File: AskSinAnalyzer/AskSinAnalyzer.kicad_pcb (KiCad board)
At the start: 2 copper layers, 87.6 x 57.8 mm, 14 parts, among them J1 Supply, SW1 SW_DIP_x04, SW2 SW_Push, U1 ESP-WROOM-32_DEVKIT_V4, U2 Arduino_Pro_Mini, U3 CC1101, U4 TJCTM24028-SPI

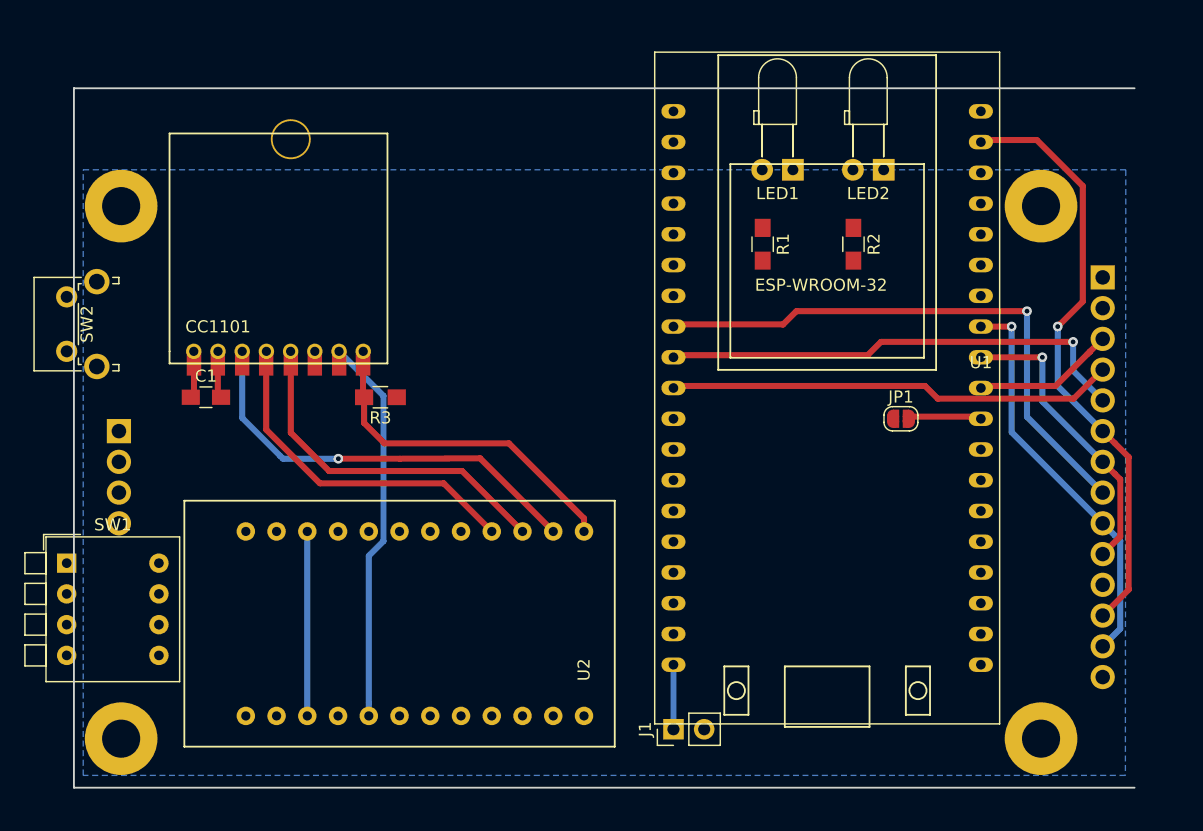
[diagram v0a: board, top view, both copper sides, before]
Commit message: AskSinAnalyzer PCB
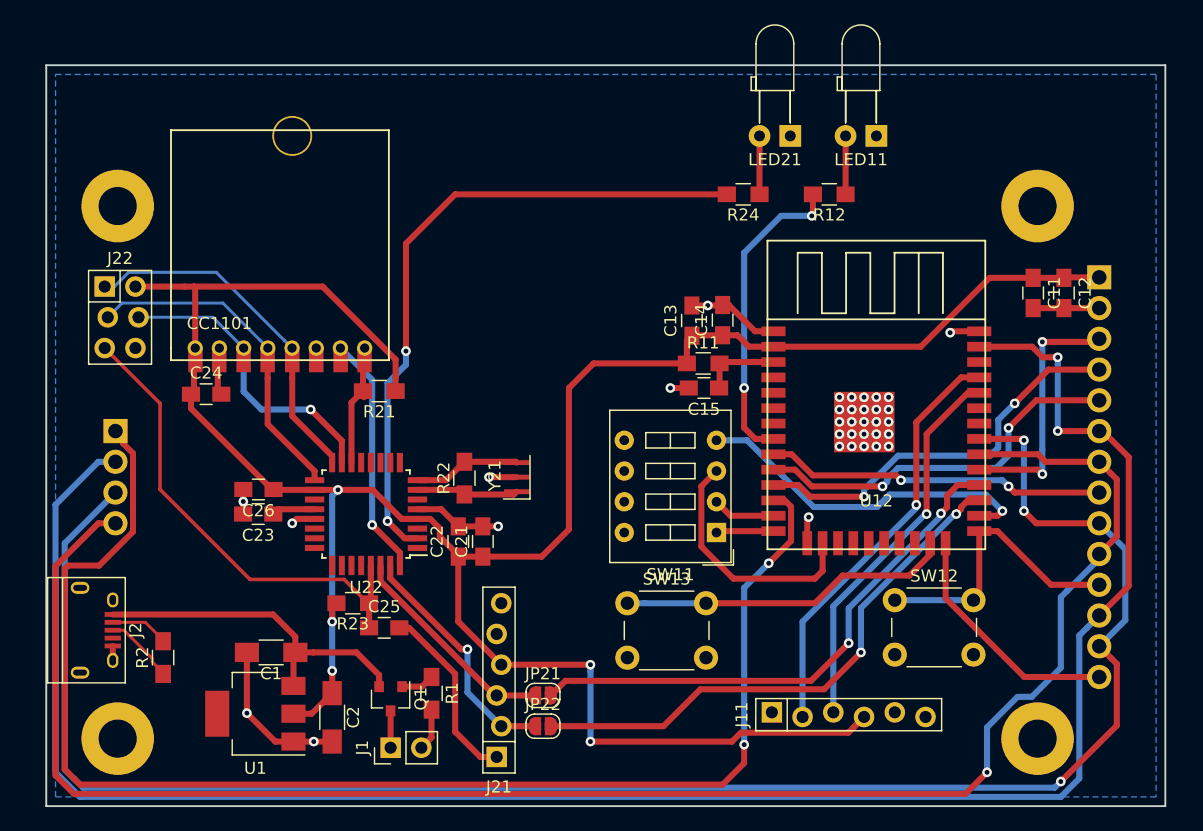
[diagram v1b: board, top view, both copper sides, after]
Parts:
- removed JP1: ~, Jumper:SolderJumper-2_P1.3mm_Open_RoundedPad1.0x1.5mm
- removed LED1: GREEN, LEDs:LED_D3.0mm_Horizontal_O3.81mm_Z6.0mm
- removed LED2: YELLOW, LEDs:LED_D3.0mm_Horizontal_O3.81mm_Z6.0mm
- removed R3: 10k, Resistors_SMD:R_0805_HandSoldering
- removed SW1: SW_DIP_x04, Buttons_Switches_THT:SW_DIP_x4_W7.62mm_Piano
- removed SW2: SW_Push, Buttons_Switches_THT:SW_Tactile_SPST_Angled_PTS645Vx83-2LFS
- removed U2: Arduino_Pro_Mini, myArduinoModules:Arduino_Pro_Mini_wo_Ax
- removed U3: CC1101, CC1101_Module:CC1101_Module
- removed U4: TJCTM24028-SPI, myDisplays:TJCTM24028-SPI
- added C11: 10u, Capacitors_SMD:C_0805_HandSoldering, F.Cu at (117.3, 105.2)
- added C12: 100n, Capacitors_SMD:C_0805_HandSoldering, F.Cu at (119.9, 105.2)
- added C13: 10u, Capacitors_SMD:C_0805_HandSoldering, F.Cu at (89.2, 107.5)
- added C14: 100n, Capacitors_SMD:C_0805_HandSoldering, F.Cu at (91.7, 107.4)
- added C15: 100n, Capacitors_SMD:C_0805_HandSoldering, F.Cu at (90.2, 113.0)
- added C2: 22u, Capacitors_SMD:C_1206_HandSoldering, F.Cu at (59.4, 140.2)
- added C21: 10u, Capacitors_SMD:C_0805_HandSoldering, F.Cu at (71.9, 125.7)
- added C22: 100n, Capacitors_SMD:C_0805_HandSoldering, F.Cu at (69.8, 125.7)
- added C23: 100n, Capacitors_SMD:C_0805_HandSoldering, F.Cu at (53.3, 123.4)
- added C24: 1u, Capacitors_SMD:C_0805_HandSoldering, F.Cu at (49.0, 113.5)
- added C25: 100n, Capacitors_SMD:C_0805_HandSoldering, F.Cu at (63.7, 132.8)
- added C26: 100n, Capacitors_SMD:C_0805_HandSoldering, F.Cu at (53.3, 121.4)
- added J11: FTDI_ESP, myPinHeaders:Pin_Header_Straight_1x06_Pitch2.54mm_Tight_Fit, F.Cu at (102.1, 140.0)
- added J2: USB_B_Micro, Connectors:USB_Micro-B, F.Cu at (40.0, 133.0)
- added J21: FTDI_ATmega, myPinHeaders:Pin_Header_Straight_1x06_Pitch2.54mm_Tight_Fit, F.Cu at (73.2, 137.2)
- added J22: AVR-ISP-6, myPinHeaders:Pin_Header_Straight_2x03_Pitch2.54mm_Tight_Fit, F.Cu at (40.6, 104.6)
- added JP21: ~, Jumper:SolderJumper-2_P1.3mm_Open_RoundedPad1.0x1.5mm, F.Cu at (76.8, 138.4)
- added JP22: ~, Jumper:SolderJumper-2_P1.3mm_Open_RoundedPad1.0x1.5mm, F.Cu at (76.8, 141.0)
- added LED11: YELLOW, LEDs:LED_D3.0mm_Horizontal_O3.81mm_Z6.0mm, F.Cu at (104.4, 92.2)
- added LED21: GREEN, LEDs:LED_D3.0mm_Horizontal_O3.81mm_Z6.0mm, F.Cu at (97.3, 92.2)
- added Q1: IRLML5203, TO_SOT_Packages_SMD:SOT-23, F.Cu at (64.3, 138.7)
- added R11: 10k, Resistors_SMD:R_0805_HandSoldering, F.Cu at (90.1, 111.0)
- added R12: 330, Resistors_SMD:R_0805_HandSoldering, F.Cu at (100.5, 97.0)
- added R21: 10k, Resistors_SMD:R_0805_HandSoldering, F.Cu at (63.3, 113.3)
- added R22: 1M, Resistors_SMD:R_0805_HandSoldering, F.Cu at (70.4, 120.5)
- added R23: 10k, Resistors_SMD:R_0805_HandSoldering, F.Cu at (61.1, 130.8)
- added R24: 330, Resistors_SMD:R_0805_HandSoldering, F.Cu at (93.4, 97.0)
- added SW11: DIP4, Buttons_Switches_THT:SW_DIP_x4_W7.62mm_Slide, F.Cu at (91.2, 125.0)
- added SW12: Flash, Buttons_Switches_THT:SW_PUSH_6mm, F.Cu at (105.9, 130.6)
- added SW13: Button, Buttons_Switches_THT:SW_PUSH_6mm, F.Cu at (83.8, 130.8)
- added U11: TJCTM24028-SPI, myDisplays:TJCTM24028-SPI, B.Cu at (124.7, 95.0)
- added U12: ESP-WROOM-32, myEspModules:ESP-WROOM-32, F.Cu at (104.4, 117.1)
- added U21: CC1101, CC1101_Module:CC1101_Module, F.Cu at (55.1, 109.7)
- added U22: ATmega328PB-AU, myHousings:TQFP-32_7x7mm_Pitch0.8mm_HandSoldering, F.Cu at (62.2, 123.4)
- added Y21: 8MHz, myResonators:Resonator_SMD_muRata_TPSKA-3pin_7.9x3.8mm_HandSoldering, F.Cu at (74.7, 120.4)
- C1: value 1u -> 22u; footprint Capacitors_SMD:C_0805_HandSoldering -> Capacitors_SMD:C_1206_HandSoldering
- R1: value 330 -> 100k
- R2: value 330 -> 200
- U1: value ESP-WROOM-32_DEVKIT_V4 -> LM1117-3.3; footprint myEspModules:ESP-WROOM-32_DEVKIT_V4 -> TO_SOT_Packages_SMD:SOT-223
- moved R2 66.5 mm to (45.5, 135.3), turned to 90 degrees
- moved U1 54.4 mm to (53.1, 139.9), turned to 180 degrees
- moved R1 46.1 mm to (67.6, 138.3)
- moved J1 23.4 mm to (64.3, 142.7)
- moved C1 21.8 mm to (54.4, 134.9), turned to 180 degrees
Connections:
- C1 pad 1: +3V3 -> +5V
- J1 pad 1: +5V -> Net-(J1-Pad1)
- R1 pad 2: /LED_RX -> GND
- R2 pad 2: /LED_AP -> Net-(J2-Pad2)
- U1 pad 2: Net-(U1-Pad2) -> +3V3
- U1 pad 4: /SW_UNUSED -> (no net)
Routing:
- net +3V3: track 2.90 -> 204.5 mm, vias 0 -> 5
- net /sheetEsp/SD_TFT_MOSI: track 0.00 -> 162.2 mm, vias 0 -> 2
- net /sheetEsp/SD_TFT_MISO: track 0.00 -> 149.6 mm, vias 0 -> 3
- net /sheetEsp/SD_TFT_SCK: track 0.00 -> 143.6 mm, vias 0 -> 1
- net /sheetEsp/SD_CS: track 0.00 -> 114.2 mm, vias 0 -> 2
- net /sheetAtmega/LED_RX: track 0.00 -> 54.8 mm, vias 0 -> 2
- net GND: track 3.28 -> 53.6 mm, vias 0 -> 35
- net /SD_TFT_MOSI: track 49.8 -> 0.00 mm, vias 1 -> 0
- net /TFT_LED: track 47.4 -> 0.00 mm, vias 1 -> 0
- net /sheetAtmega/ATmega_TX: track 0.00 -> 45.4 mm, vias 0 -> 2
- net /sheetAtmega/ATmega_RX: track 0.00 -> 44.9 mm, vias 0 -> 2
- net /sheetAtmega/RESET: track 0.00 -> 40.0 mm
- net /TFT_DC: track 39.4 -> 0.00 mm, vias 1 -> 0
- net /TFT_RESET: track 37.0 -> 0.00 mm
- net /MOSI: track 35.1 -> 0.00 mm, vias 1 -> 0
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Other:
- board size 87.6 x 57.8 mm -> 92.5 x 61.2 mm
- board text added: "ToDo: - antenna connector - labels - mounting holes"

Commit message: PCB update
reference labels moved
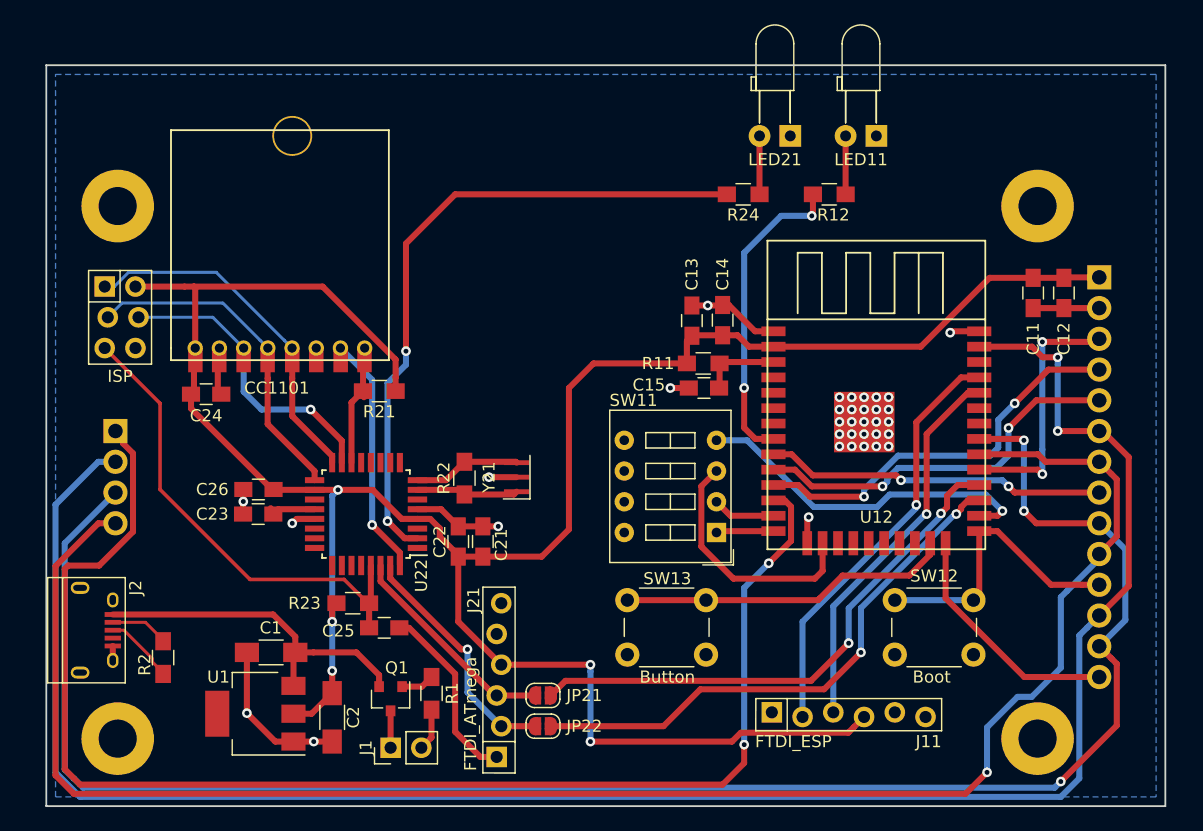
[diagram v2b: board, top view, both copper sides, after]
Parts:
- J22: value AVR-ISP-6 -> ISP
- SW12: value Flash -> Boot
- moved SW13 0.25 mm to (83.8, 130.6)

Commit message: antenna added
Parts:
- added J23: Conn_Coaxial, Connectors:SMA_THT_Jack_Straight, F.Cu at (56.1, 90.7)
- U21: footprint CC1101_Module:CC1101_Module -> myRadioModules:CC1101_SMD_THT_Antenna
- Y21: value 8MHz -> 8M; footprint myResonators:Resonator_SMD_muRata_TPSKA-3pin_7.9x3.8mm_HandSoldering -> myResonators:Resonator_SMD_muRata_CSTCC-3pin_7.2x3.0mm_HandSoldering
- moved U21 4.83 mm to (55.1, 114.6)
- moved C24 4.57 mm to (49.0, 118.1)
- moved R21 2.43 mm to (65.5, 114.3), turned to 270 degrees
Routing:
- net /sheetAtmega/MISO: track 28.4 -> 47.0 mm
- net /sheetAtmega/GDO0: track 20.0 -> 15.2 mm
- net Net-(J23-Pad1): track 0.00 -> 4.63 mm
- net +3V3: track 204.5 -> 207.6 mm
- net /sheetAtmega/CS: track 9.13 -> 7.97 mm
- net GND: track 53.6 -> 53.0 mm
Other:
- board text added: "+-"
- board text added: "AskSin Analyzer"
- board text added: "ToDo: - check pads and mounting"
- board text added: "stan23 June 2019 V0.1 CC BY-NC-SA"
- board text removed: "ToDo: - antenna connector - labels - mounting holes"

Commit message: new microUSB connector
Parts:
- J2: footprint Connectors:USB_Micro-B -> myConnectors:USB_Micro
- moved J2 3.89 mm to (36.1, 133.0), turned to 0 degrees
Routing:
- net /sheetEsp/SD_TFT_SCK: track 143.6 -> 132.4 mm
- net GND: track 53.0 -> 64.1 mm, vias 35 -> 37
- net /sheetEsp/SD_CS: track 114.2 -> 103.7 mm
- net Net-(J2-Pad2): track 4.86 -> 8.90 mm
- net +5V: track 28.6 -> 32.6 mm, vias 0 -> 2
- net Net-(J2-Pad3): track 5.88 -> 8.33 mm
- net /sheetEsp/SD_TFT_MISO: track 149.6 -> 148.5 mm

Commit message: PCB update
pads for ESP made longer
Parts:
- U12: footprint myEspModules:ESP-WROOM-32 -> myEspModules:ESP-WROOM-32_handsoldering
- moved C2 0.26 mm to (59.7, 140.2)
- moved C1 0.25 mm to (54.4, 134.6)
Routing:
- net /sheetEsp/BUTTON1: track 27.5 -> 28.8 mm
- net /sheetEsp/SD_TFT_MISO: track 148.5 -> 149.6 mm
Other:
- board text removed: "ToDo: - check pads and mounting"

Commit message: AskSinAnalyzer PCB V2.0
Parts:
- removed JP21, JP22: ~, Jumper:SolderJumper-2_P1.3mm_Open_RoundedPad1.0x1.5mm
- added C3: 10n, Capacitors_SMD:C_0805_HandSoldering, F.Cu at (43.4, 128.1)
- added C4: 100n, Capacitors_SMD:C_0805_HandSoldering, F.Cu at (78.4, 90.4)
- added C5: 100n, Capacitors_SMD:C_0805_HandSoldering, F.Cu at (84.6, 98.6)
- added C6: 4u7, Capacitors_Tantalum_SMD:CP_Tantalum_Case-B_EIA-3528-21_Hand, F.Cu at (68.5, 98.2)
- added C7: 100n, Capacitors_SMD:C_0805_HandSoldering, F.Cu at (71.4, 98.2)
- added FB1: Ferrite_Bead, Resistors_SMD:R_0805_HandSoldering, F.Cu at (45.5, 128.1)
- added JP1: ~, Jumper:SolderJumper-2_P1.3mm_Open_RoundedPad1.0x1.5mm, F.Cu at (77.6, 138.4)
- added JP2: ~, Jumper:SolderJumper-2_P1.3mm_Open_RoundedPad1.0x1.5mm, F.Cu at (77.6, 141.0)
- added Q11: BC817, TO_SOT_Packages_SMD:SOT-23_Handsoldering, F.Cu at (77.5, 110.0)
- added Q12: BC817, TO_SOT_Packages_SMD:SOT-23_Handsoldering, F.Cu at (84.6, 110.0)
- added R13: 10k, Resistors_SMD:R_0805_HandSoldering, F.Cu at (80.3, 112.9)
- added R14: 10k, Resistors_SMD:R_0805_HandSoldering, F.Cu at (80.3, 107.1)
- added R15: 10k, Resistors_SMD:R_0805_HandSoldering, F.Cu at (73.9, 112.9)
- added SW1: SW_DPDT_x2, Buttons_Switches_THT:SW_CuK_JS202011CQN_DPDT_Straight, F.Cu at (67.9, 104.4)
- added SW14: Reset, Buttons_Switches_THT:SW_PUSH_6mm, F.Cu at (95.1, 130.6)
- added U2: FT232RL, myHousings:SSOP-28_5.3x10.2mm_Pitch0.65mm_Handsoldering, F.Cu at (78.4, 97.3)
- C1, C2: footprint Capacitors_SMD:C_1206_HandSoldering -> Capacitors_Tantalum_SMD:CP_Tantalum_Case-B_EIA-3528-21_Hand
- Q1: footprint TO_SOT_Packages_SMD:SOT-23 -> TO_SOT_Packages_SMD:SOT-23_Handsoldering
- U22: value ATmega328PB-AU -> ATmega328P-AU
- Y21: footprint myResonators:Resonator_SMD_muRata_CSTCC-3pin_7.2x3.0mm_HandSoldering -> myResonators:Resonator_SMD_muRata_CSTCC-CSTCE-universal-3pin_7.2x3.0mm_HandSoldering
- moved J11 2.33 mm to (103.8, 141.7), turned to 270 degrees
- moved C1 1.16 mm to (53.3, 134.1)
- moved Y21 1.14 mm to (75.7, 119.9)
- moved R22 0.69 mm to (69.8, 120.0)
- turned C21 to 270 degrees
- turned C22 to 270 degrees
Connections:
- net /sheetEsp/RX renamed /sheetEsp/ESP_RX
- net /sheetEsp/SW_DETAIL renamed /sheetEsp/SW1_DETAIL
- net /sheetEsp/SW_LINES renamed /sheetEsp/SW3_LINES
- net /sheetEsp/SW_ONLINE renamed /sheetEsp/SW2_ONLINE
- net /sheetEsp/SW_UNUSED renamed /sheetEsp/SW4_UNUSED
- net /sheetEsp/TX renamed /sheetEsp/ESP_TX
- net Net-(J2-Pad2) renamed /sheetSupply/D-
- net Net-(J2-Pad3) renamed /sheetSupply/D+
- J2 pad 1: +5V -> Net-(C3-Pad1)
- J21 pad 2: /sheetAtmega/TX -> /sheetAtmega/ATmega_TX
- J21 pad 3: /sheetAtmega/RX -> /sheetAtmega/ATmega_RX
- U12 pad 27: /sheetAtmega/ATmega_TX -> /sheetEsp/ESP_RX2
- U12 pad 28: /sheetAtmega/ATmega_RX -> /sheetEsp/ESP_TX2
- U22 pad 3: (no net) -> GND
- U22 pad 30: /sheetAtmega/RX -> /sheetAtmega/ATmega_RX
- U22 pad 31: /sheetAtmega/TX -> /sheetAtmega/ATmega_TX
- U22 pad 6: (no net) -> +3V3
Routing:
- net /sheetSupply/D+: track 8.33 -> 81.2 mm, vias 0 -> 2
- net /sheetSupply/D-: track 8.90 -> 80.4 mm, vias 0 -> 2
- net +5V: track 32.6 -> 93.4 mm
- net /sheetEsp/ESP_RX2: track 0.00 -> 48.8 mm, vias 0 -> 2
- net /sheetEsp/ESP_TX2: track 0.00 -> 48.7 mm, vias 0 -> 2
- net /sheetEsp/T_CS: track 24.1 -> 71.8 mm
- net /sheetEsp/ESP_RX: track 32.1 -> 79.2 mm, vias 1 -> 3
- net GND: track 64.1 -> 106.8 mm, vias 37 -> 41
- net /sheetEsp/ESP_TX: track 35.0 -> 77.6 mm, vias 1 -> 2
- net /sheetEsp/EN: track 6.55 -> 42.8 mm
- net +3V3: track 207.6 -> 241.7 mm, vias 5 -> 7
- net /sheetAtmega/TX: track 20.2 -> 0.00 mm, vias 1 -> 0
- net /sheetAtmega/RX: track 18.0 -> 0.00 mm
- net /sheetEsp/ESP_RTS: track 0.00 -> 15.8 mm
- net Net-(SW1-Pad5): track 0.00 -> 15.2 mm
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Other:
- net class Supply added: clearance 0.2, trace_width 0.5, via_dia 1, via_drill 0.5
- board text added: "ATmega"
- board text added: "DTR RX TX VCC GND GND"
- board text added: "ESP"
- board text added: "GND GND VCC TX RX DTR"
- board text added: "Unused Lines Online Details"
- board text added: "stan23 Sept 2019 V2.0 CC BY-NC-SA"
- board text removed: "stan23 June 2019 V0.1 CC BY-NC-SA"
